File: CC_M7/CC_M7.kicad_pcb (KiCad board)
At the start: 4 copper layers, 40 x 65 mm, 129 parts, among them J1 Conn_01x04_Pin, J10 Conn_01x04_Pin, J11 USB_B_Micro, J12 Conn_01x04_Pin, J13 Batt_Pins, J3 Conn_01x03_Pin, J4 Conn_01x03_Pin, J5 Conn_01x03_Pin, J6 Conn_01x03_Pin, J7 Conn_01x03_Pin, J8 Conn_01x03_Pin, J9 SMA_CONNECTOR, U1 STM32H743VITx, U10 ME6211C33M5, U11 BMP581, U12 IIM-42652, U2 24AA64T-I/OT, U3 BMI088, U4 ICP-20100, U5 BMM150, U6 nRF52820-QDxx, U7 NRF21540-QDAA-R7, U8 TPS562246DRLR, U9 ME6211C33M5, Y1 32MHz, Y2 32MHz

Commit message: Scehmatic completed.
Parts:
- removed C26, C27: 100nF, Capacitor_SMD:C_0402_1005Metric
- removed L2: 15nH, Inductor_SMD:L_0402_1005Metric
- removed L3: 3.3uH, Inductor_SMD:L_Changjiang_FXL0650
- added C58: 1pF, Capacitor_SMD:C_0402_1005Metric, F.Cu at (144.3, 138.3)
- added C59: 10nF, Capacitor_SMD:C_0402_1005Metric, F.Cu at (144.3, 134.3)
- added R18: 33k, Resistor_SMD:R_0402_1005Metric, F.Cu at (144.3, 132.3)
- added U13: ICM-20948, Sensor_Motion:InvenSense_QFN-24_3x3mm_P0.4mm, F.Cu at (138.3, 133.9)
- C20, C21: value 16pF -> 12pF
- C34: value 4.7uF -> 10uF
- C35: value 820pF -> 10uF; footprint Capacitor_SMD:C_0201_0603Metric -> Capacitor_SMD:C_0603_1608Metric
- C37: value 47nF -> 0
- C43: value 10uF -> 100nF; footprint Capacitor_SMD:C_1206_3216Metric -> Capacitor_SMD:C_0402_1005Metric
- C47: value 100nF -> 33pF
- C49: value 47pF -> 22uH; footprint Capacitor_SMD:C_0402_1005Metric -> Capacitor_SMD:C_0603_1608Metric
- C52: value 2.2uF -> 100nF
- C53: value 10nF -> 10uF; footprint Capacitor_SMD:C_0402_1005Metric -> Capacitor_SMD:C_0603_1608Metric
- C56: value 22uF -> 100nF; footprint Capacitor_SMD:C_0805_2012Metric -> Capacitor_SMD:C_0402_1005Metric
- C57: value 10uF -> 100nF; footprint Capacitor_SMD:C_0805_2012Metric -> Capacitor_SMD:C_0402_1005Metric
- L1: value 10uH -> 2.2uH; footprint Inductor_SMD:L_0603_1608Metric -> Inductor_SMD:L_0402_1005Metric
- R10: value 100K -> 100k; footprint Resistor_SMD:R_0603_1608Metric -> Resistor_SMD:R_0402_1005Metric
- R11: value 1k -> 10k
- R12: value 220K -> 33.2k; footprint Resistor_SMD:R_0603_1608Metric -> Resistor_SMD:R_0402_1005Metric
- R13: value 30K -> 220k; footprint Resistor_SMD:R_0603_1608Metric -> Resistor_SMD:R_0402_1005Metric
- U1: value STM32H743VITx -> STM32H743VGTx
- U12: value IIM-42652 -> TPS79318-EP; footprint Package_LGA:Bosch_LGA-14_3x2.5mm_P0.5mm -> Package_TO_SOT_SMD:SOT-23-5
- U5: value BMM150 -> TXB0104RUT; footprint Package_CSP:WLCSP-12_1.56x1.56mm_P0.4mm -> Package_DFN_QFN:Texas_R-PUQFN-N12
- U8: value TPS562246DRLR -> TPS562206; footprint TPS562246DRLR:DRL0006A-MFG -> Package_TO_SOT_SMD:SOT-563
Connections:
- C34 pad 1: USBDEC -> +BATT
- C35 pad 1: DEC5 -> +BATT
- C43 pad 1: GND -> +BATT
- C43 pad 2: +BATT -> GND
- C47 pad 1: GND -> Net-(C47-Pad1)
- C47 pad 2: +BATT -> Net-(U8-VFB)
- C48 pad 1: Net-(U8-SW) -> +3.3V
- C48 pad 2: Net-(U8-BST) -> GND
- C49 pad 1: Net-(U8-FB) -> Net-(C47-Pad1)
- C49 pad 2: Net-(U8-SW) -> GND
- C51 pad 1: +3.3V -> Net-(C47-Pad1)
- C52 pad 1: +3.3V -> +1V8
- C53 pad 1: +3.3V -> +1V8
- C56 pad 1: GND -> +1V8
- C56 pad 2: Net-(C56-Pad2) -> GND
- C57 pad 1: GND -> Net-(U13-REGOUT)
- C57 pad 2: +BATT -> GND
- D1 pad A: Net-(C56-Pad2) -> Net-(C47-Pad1)
- D1 pad K: VIN_5V -> +5V
- L1 pad 1: DCC -> Net-(U8-SW)
- L1 pad 2: Net-(L1-Pad2) -> Net-(C47-Pad1)
- R10 pad 1: Net-(U8-EN) -> +BATT
- R10 pad 2: +BATT -> Net-(U8-EN)
- R11 pad 1: Net-(U5-DRDY) -> GND
- R11 pad 2: I2C1_IRQ2 -> +1V8
- R12 pad 1: Net-(C56-Pad2) -> Net-(U8-EN)
- R12 pad 2: Net-(U8-FB) -> GND
- R13 pad 1: Net-(U8-FB) -> Net-(C47-Pad1)
- R13 pad 2: GND -> Net-(U8-VFB)
- U1 pad 45: I2C1_IRQ3 -> unconnected-(U1-PE15-Pad45)
- U11 pad 5: unconnected-(U11-SDO-Pad5) -> GND
- U12 pad 1: SPI1_MISO -> +3.3V
- U12 pad 2: unconnected-(U12-RESV-Pad2) -> GND
- U12 pad 3: unconnected-(U12-RESV-Pad3) -> +3.3V
- U12 pad 4: unconnected-(U12-INT1/INT-Pad4) -> Net-(U12-BP)
- U12 pad 5: +3.3V -> +1V8
- U4 pad 7: I2C1_IRQ3 -> I2C1_IRQ2
- U6 pad 10: unconnected-(U6-VBUS-Pad10) -> GND
- U6 pad 11: USBDEC -> unconnected-(U6-DECUSB-Pad11)
- U6 pad 21: DEC5 -> unconnected-(U6-DEC5-Pad21)
- U7 pad 10: NRF_ANT -> Net-(U7-TRX)
- U8 pad 4: Net-(U8-BST) -> GND
- U8 pad 6: Net-(U8-FB) -> Net-(U8-VFB)
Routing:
- net I2C1_IRQ2: track 15.5 -> 27.8 mm, vias 2 -> 4
- net I2C1_IRQ3: track 12.2 -> 0.00 mm, vias 2 -> 0
- net USBDEC: track 3.74 -> 0.00 mm, vias 1 -> 0
- net +BATT: track 22.7 -> 26.5 mm, vias 1 -> 2
- net Net-(L1-Pad2): track 1.52 -> 0.00 mm
- net Net-(C47-Pad1): track 0.00 -> 1.52 mm
- net GND: track 178.1 -> 179.1 mm, vias 28 -> 30
- net Net-(U8-BST): track 1.08 -> 0.00 mm, vias 1 -> 0
- net Net-(U5-DRDY): vias 1 -> 0

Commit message: ready for routing
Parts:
- removed D1: MBR230LSFT1G, MBR230LSFT1G:SODFL3619X98N
- added D7: 1N5819WS, Diode_SMD:D_SOD-323, F.Cu at (99.4, 182.2)
- added D8: 1N5819WS, Diode_SMD:D_SOD-323, F.Cu at (102.8, 182.2)
- added D9: SS210, Diode_SMD:D_SOD-123, F.Cu at (117.1, 184.3)
- added JP10: SWDIO, Jumper:SolderJumper-2_P1.3mm_Open_TrianglePad1.0x1.5mm, F.Cu at (63.3, 103.8)
- added JP9: SWDIO, Jumper:SolderJumper-2_P1.3mm_Open_TrianglePad1.0x1.5mm, F.Cu at (63.3, 100.2)
- C1: footprint Capacitor_SMD:C_0603_1608Metric -> Capacitor_SMD:C_0402_1005Metric; moved to F.Cu
- C10, C11, C12, C13, C14, C15, C16, C17, C18, C19, C2, C20, C21, C22, C23, C24, C25, C3, C30, C34, C35, C39, C4, C40, C46, C48, C5, C51, C52, C53, C54, C55, C6, C7, C8, C9, FB1, R1, R10, R11, R12, R13, R14, R15, R16, R17, R2, R4, R5, R6, R7, R8, R9: moved to F.Cu
- C28, C29, C33: footprint Capacitor_SMD:C_0201_0603Metric -> Capacitor_SMD:C_0402_1005Metric
- C31, C32, C37, C38, C41, C42, C44: footprint Capacitor_SMD:C_0201_0603Metric -> Capacitor_SMD:C_0402_1005Metric; moved to F.Cu
- JP1, JP2, JP3, JP4, JP5, JP6, JP7, JP8: footprint jmpertest:jmpertest -> Jumper:SolderJumper-2_P1.3mm_Open_TrianglePad1.0x1.5mm
- moved R2 91.3 mm to (190.0, 126.7), turned to 180 degrees
- moved C37 89.1 mm to (190.8, 130.4), turned to 0 degrees
- moved C39 86.5 mm to (190.0, 133.2), turned to 180 degrees
- moved C40 86.0 mm to (190.3, 137.2), turned to 180 degrees
- moved C31 85.7 mm to (190.8, 128.6), turned to 0 degrees
- moved C38 83.6 mm to (190.0, 134.1), turned to 0 degrees
- moved C32 82.8 mm to (190.8, 129.5), turned to 180 degrees
- moved C20 82.3 mm to (178.3, 138.0)
- moved C21 82.3 mm to (178.3, 138.9), turned to 0 degrees
- moved C15 80.8 mm to (176.8, 144.1), turned to 0 degrees
- moved C16 80.8 mm to (176.9, 145.1), turned to 0 degrees
- moved C44 77.7 mm to (178.4, 139.8), turned to 180 degrees
- moved C41 77.0 mm to (190.0, 135.0), turned to 0 degrees
- moved C42 76.9 mm to (190.0, 136.0), turned to 0 degrees
- moved C14 75.6 mm to (175.4, 144.3), turned to 90 degrees
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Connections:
- C45 pad 1: 3V3_RF -> Net-(D8-A)
- C50 pad 1: +3.3V -> Net-(D7-A)
- J2 pad 29: PE6 -> unconnected-(J2-Pin_29-Pad29)
- J2 pad 31: PE5 -> J2_31
- J2 pad 34: GND -> J2_34
- J2 pad 38: J2_38 -> unconnected-(J2-Pin_38-Pad38)
- JP1 pad 1: SWO -> +3.3V
- JP1 pad 2: J2_32 -> J2_31
- JP2 pad 1: SWCLK -> SWDIO
- JP2 pad 2: J2_36 -> J2_32
- JP3 pad 1: SWDIO -> SWCLK
- JP3 pad 2: J2_38 -> J2_34
- JP4 pad 1: NRST -> SWO
- JP4 pad 2: J2_40 -> J2_36
- JP5 pad 1: 3V3_RF -> NRST
- JP5 pad 2: J2_32 -> J2_40
- JP6 pad 1: NRF_SWCLK -> J2_31
- JP6 pad 2: J2_36 -> 3V3_RF
- JP7 pad 1: NRF_SWDIO -> J2_32
- JP7 pad 2: J2_38 -> NRF_SWDIO
- JP8 pad 1: NRF_NRST -> J2_34
- JP8 pad 2: J2_40 -> NRF_SWCLK
- U1 pad 4: PE5 -> unconnected-(U1-PE5-Pad4)
- U1 pad 5: PE6 -> unconnected-(U1-PE6-Pad5)
- U10 pad 5: +3.3V -> Net-(D7-A)
- U9 pad 5: 3V3_RF -> Net-(D8-A)
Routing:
- net GND: track 179.1 -> 52.7 mm, vias 30 -> 0
- net +3.3V: track 78.6 -> 26.2 mm, vias 17 -> 0
- net USB_DP: track 59.0 -> 18.5 mm, vias 2 -> 0
- net USB_DM: track 57.4 -> 20.5 mm, vias 2 -> 0
- net NRST: track 55.1 -> 32.7 mm, vias 4 -> 0
- net +5V: track 81.1 -> 68.5 mm, vias 2 -> 0
- net Net-(C56-Pad2): track 12.2 -> 0.00 mm, vias 1 -> 0
- net (no net): track 0.00 -> 12.2 mm
- net J2_38: track 11.0 -> 0.00 mm, vias 1 -> 0
- net +BATT: track 26.5 -> 16.7 mm, vias 2 -> 0
- net unconnected-(J2-Pin_38-Pad38): track 0.00 -> 9.34 mm
- net PE5: track 7.99 -> 0.00 mm, vias 1 -> 0
- net PE6: track 7.58 -> 0.00 mm, vias 1 -> 0
- net J2_31: track 0.00 -> 6.80 mm
- net NRF_SWCLK: track 18.4 -> 11.8 mm, vias 2 -> 0
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
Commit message: ready for routing
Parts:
- D9: footprint Diode_SMD:D_SOD-123 -> Diode_SMD:D_SOD-323
- moved D9 0.75 mm to (117.9, 184.3)

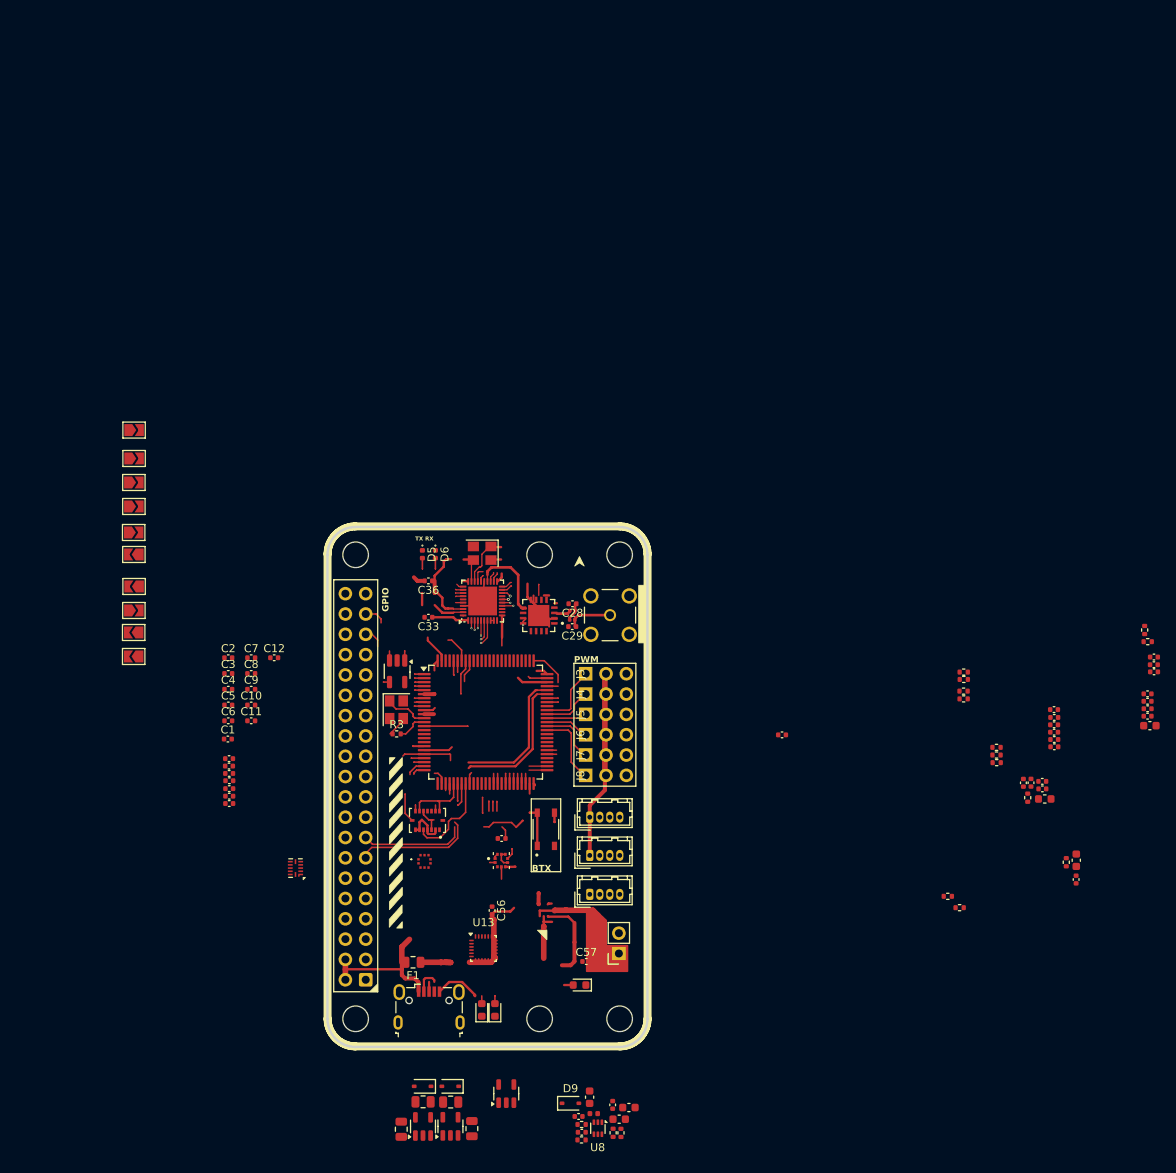
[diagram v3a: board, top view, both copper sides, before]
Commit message: ready to routing
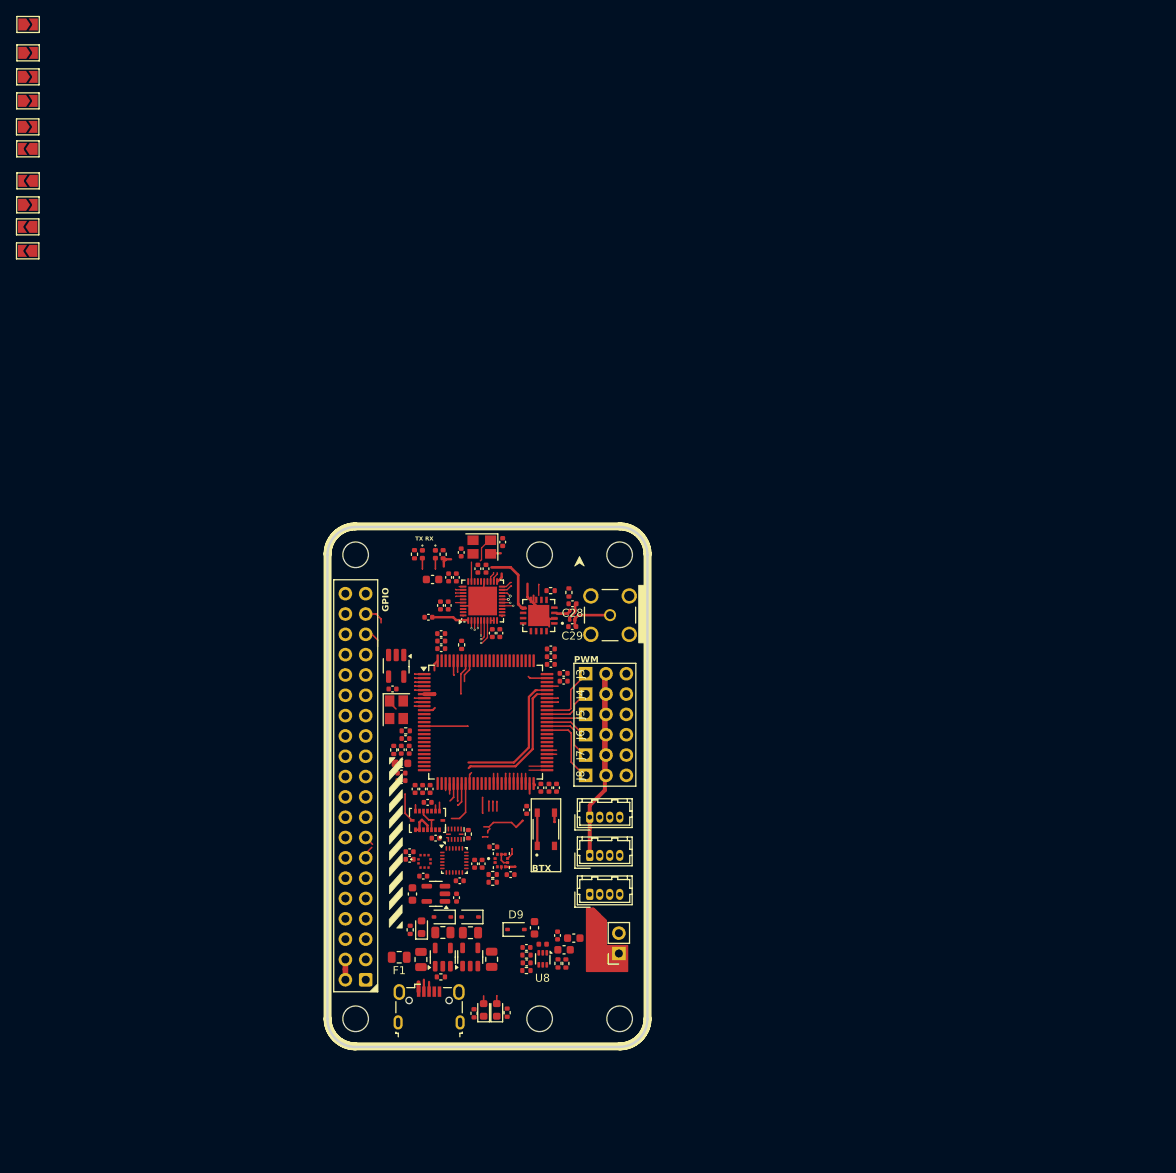
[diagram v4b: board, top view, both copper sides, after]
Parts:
- moved R2 92.3 mm to (98.4, 115.7), turned to 90 degrees
- moved C40 91.5 mm to (100.6, 118.9), turned to 0 degrees
- moved C37 89.6 mm to (101.6, 122.1), turned to 90 degrees
- moved C42 89.1 mm to (102.6, 118.6), turned to 90 degrees
- moved C39 87.6 mm to (103.6, 118.6), turned to -90 degrees
- moved C31 85.2 mm to (106.3, 117.5), turned to 90 degrees
- moved C53 83.1 mm to (98.1, 158.2)
- moved C20 82.9 mm to (95.6, 132.6)
- moved C32 82.8 mm to (109.4, 114.2), turned to 90 degrees
- moved C41 82.5 mm to (108.1, 125.6), turned to -90 degrees
- moved C38 81.4 mm to (109.0, 125.6), turned to -90 degrees
- moved C21 81.1 mm to (97.3, 138.8)
- moved FB1 80.5 mm to (96.7, 141.9), turned to 0 degrees
- moved C16 80.1 mm to (96.8, 144.0), turned to 180 degrees
- moved C15 80.1 mm to (96.7, 143.1), turned to 180 degrees
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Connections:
- J2 pad 10: UART2_TX -> UART4_TX
- J2 pad 16: UART4_RX -> unconnected-(J2-Pin_16-Pad16)
- J2 pad 18: UART4_TX -> unconnected-(J2-Pin_18-Pad18)
- J2 pad 33: PE4 -> UART2_TX
- J2 pad 35: PE3 -> UART2_RX
- J2 pad 8: UART2_RX -> UART4_RX
- U1 pad 2: PE3 -> unconnected-(U1-PE3-Pad2)
- U1 pad 3: PE4 -> unconnected-(U1-PE4-Pad3)
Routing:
- net GND: track 52.7 -> 29.4 mm
- net UART2_RX: track 24.4 -> 4.86 mm
- net unconnected-(J2-Pin_16-Pad16): track 0.00 -> 14.7 mm
- net +5V: track 68.5 -> 54.2 mm
- net CAN2_RX: track 31.5 -> 18.1 mm
- net UART2_TX: track 22.8 -> 10.2 mm
- net CAN2_TX: track 31.1 -> 19.1 mm
- net unconnected-(J2-Pin_18-Pad18): track 0.00 -> 11.5 mm
- net PE3: track 11.4 -> 0.00 mm
- net DEC4: track 11.3 -> 0.00 mm
- net NRF_ANT: track 10.5 -> 0.00 mm
- net PE4: track 9.21 -> 0.00 mm
- net NRF_PA_TX_EN: track 8.37 -> 16.9 mm
- net +BATT: track 16.7 -> 9.29 mm
- net VDDA_CC: track 6.81 -> 0.00 mm
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
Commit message: test
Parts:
- moved R7 0.51 mm to (101.2, 168.5)
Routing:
- net +5V: track 54.2 -> 69.3 mm
- net +BATT: track 9.29 -> 21.4 mm
- net +3.3V: track 19.7 -> 30.9 mm
- net +1V8: track 1.23 -> 9.69 mm
- net VIN_5V: track 23.8 -> 30.7 mm, vias 0 -> 1
- net Net-(D9-A): track 0.00 -> 6.44 mm
- net Net-(U8-VFB): track 0.00 -> 4.47 mm
- net Net-(U8-EN): track 0.00 -> 3.75 mm
- net Net-(D2-K): track 0.00 -> 1.45 mm
- net Net-(D3-K): track 0.00 -> 1.33 mm
- net Net-(U8-SW): track 0.00 -> 1.28 mm
- net Net-(D4-K): track 0.00 -> 1.26 mm

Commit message: ready final
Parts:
- moved C33 4.48 mm to (104.3, 125.2)
- moved C40 0.79 mm to (101.4, 119.1), turned to 90 degrees
- moved C36 0.30 mm to (102.3, 122.1)
- moved C37 0.30 mm to (101.3, 122.1)
- moved C59 0.17 mm to (99.5, 155.8)
- moved C57 0.09 mm to (104.1, 156.5)
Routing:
- net +3.3V: track 30.9 -> 18.1 mm
- net SPI1_CS2: track 5.69 -> 0.00 mm
- net SPI1_MOSI: track 19.5 -> 16.5 mm
- net SPI1_CS1: track 6.43 -> 3.51 mm
- net GND: track 29.4 -> 26.5 mm
- net SPI1_SCK: track 27.2 -> 24.7 mm
- net SPI1_MISO: track 19.6 -> 17.3 mm
- net +1V8: track 9.69 -> 8.62 mm
- net I2C1_SCL: track 68.1 -> 67.4 mm

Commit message: Routing in progress
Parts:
- moved JP1 56.9 mm to (62.1, 114.7)
- moved JP10 56.9 mm to (62.2, 108.7)
- moved JP2 56.9 mm to (62.1, 111.7)
- moved JP3 56.9 mm to (62.1, 117.9)
- moved JP6 56.9 mm to (62.1, 120.7)
- moved JP7 56.9 mm to (62.1, 133.4)
- moved JP8 56.9 mm to (62.2, 124.7)
- moved JP9 56.9 mm to (62.2, 105.1)
- moved JP4 56.4 mm to (76.3, 122.0), turned to 180 degrees
- moved JP5 51.8 mm to (76.3, 119.5)
- moved R5 32.1 mm to (137.6, 143.9), turned to -90 degrees
- moved R4 30.8 mm to (136.6, 143.9), turned to 90 degrees
- moved C19 23.6 mm to (95.4, 131.3), turned to 180 degrees
- moved F1 21.1 mm to (116.0, 158.2), turned to -90 degrees
- moved C17 16.7 mm to (110.5, 145.9), turned to 180 degrees
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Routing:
- net I2C1_SCL: track 67.4 -> 0.00 mm
- net I2C1_SDA: track 66.3 -> 0.00 mm
- net 3V3_RF: track 65.0 -> 8.39 mm, vias 1 -> 0
- net I2C2_SDA: track 40.7 -> 0.00 mm
- net UART4_RX: track 38.9 -> 0.00 mm
- net I2C2_SCL: track 37.7 -> 0.00 mm
- net UART4_TX: track 36.7 -> 0.00 mm
- net LED1: track 33.8 -> 0.98 mm
- net LED0: track 33.3 -> 0.97 mm
- net VIN_5V: track 30.7 -> 0.00 mm, vias 1 -> 0
- net NRST: track 31.8 -> 4.15 mm
- net GND: track 26.5 -> 0.00 mm
- net PA4: track 26.4 -> 0.00 mm
- net UART1_RX: track 24.7 -> 0.00 mm
- net I2C1_IRQ2: track 24.1 -> 0.00 mm
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
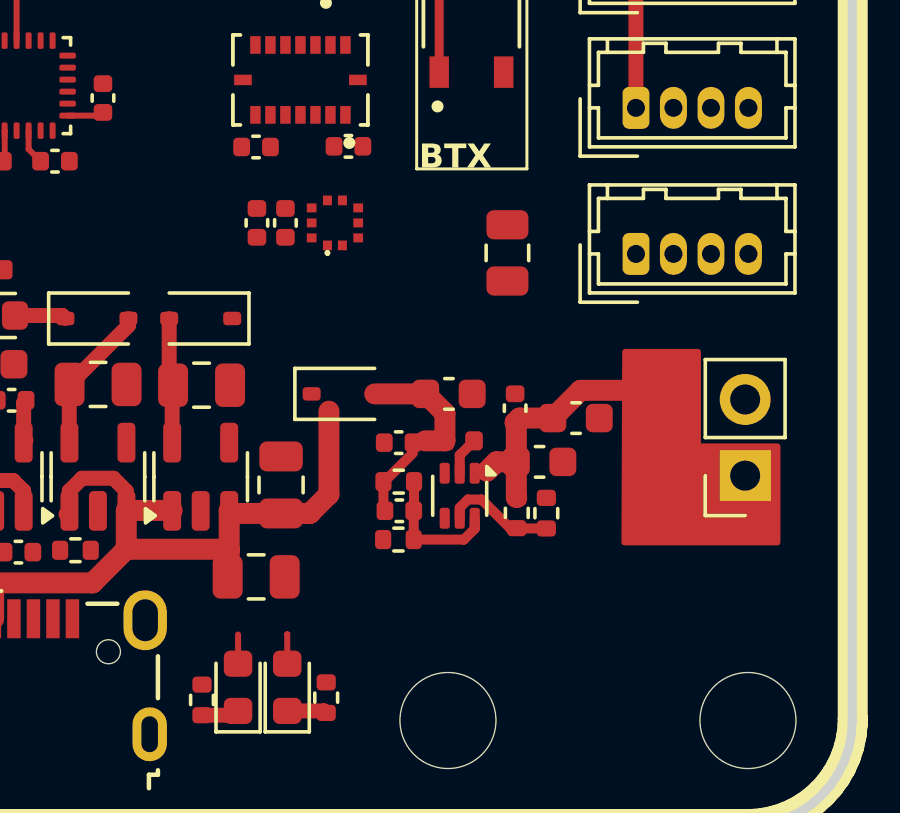
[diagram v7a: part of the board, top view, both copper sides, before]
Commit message: Inductor added.
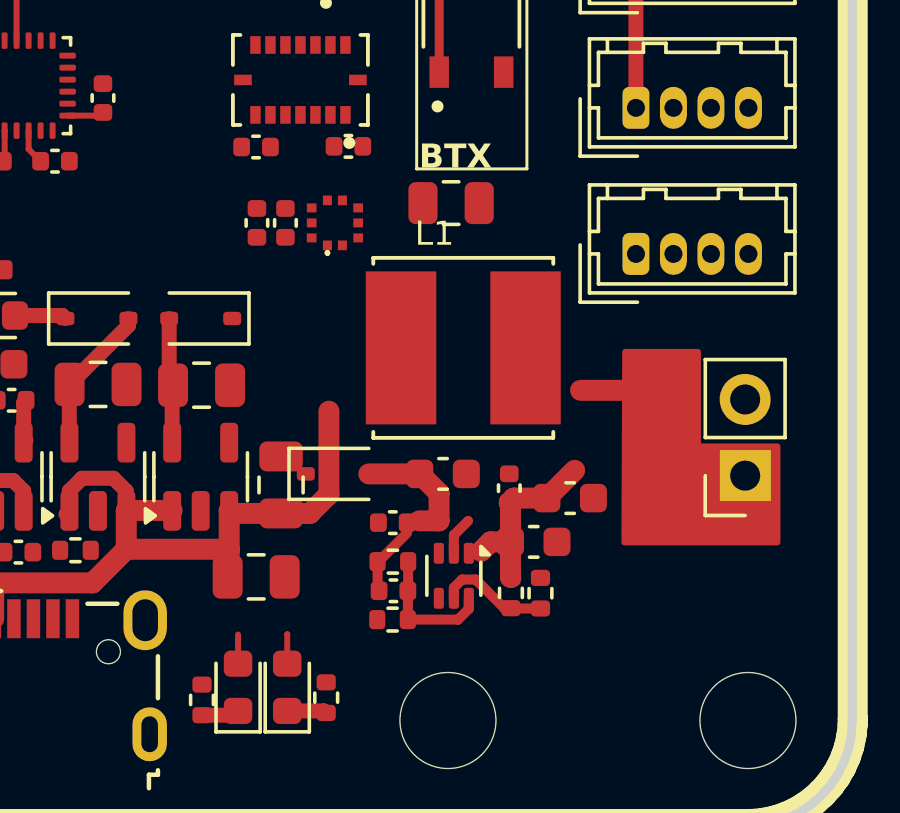
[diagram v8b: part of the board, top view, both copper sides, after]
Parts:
- L1: value 2.2uH -> SRN6045TA-2R2Y; footprint Inductor_SMD:L_0402_1005Metric -> 6x6mmIND:IND_SRN6045TA-2R2Y
- moved L1 3.10 mm to (114.5, 161.4), turned to 0 degrees
- moved C34 2.67 mm to (118.1, 166.4)
- moved C43 2.67 mm to (116.1, 166.0)
- moved C47 2.67 mm to (112.2, 169.5)
- moved C49 2.67 mm to (113.9, 165.6)
- moved C51 2.67 mm to (112.2, 167.2)
- moved D9 2.67 mm to (110.3, 165.6)
- moved R12 2.67 mm to (117.1, 169.5)
- moved R13 2.67 mm to (112.2, 168.5)
- moved R18 2.67 mm to (112.2, 170.4)
- moved U8 2.67 mm to (114.2, 169.0)
- moved C35 2.67 mm to (116.9, 167.8)
- moved R10 2.67 mm to (116.1, 169.5)
- moved F1 2.51 mm to (114.1, 156.5), turned to 0 degrees
